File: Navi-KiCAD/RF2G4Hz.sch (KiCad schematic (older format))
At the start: 39 parts, among them J5 0734120110, U3 CC2650F128RGZR, U4 CC2592RGVR, Y5 XRCGB24M000F2P00R0

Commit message: Some BOM consolidation.
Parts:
- C37: value 1n -> 0.01u
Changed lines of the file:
@@
-$EndComp
-$Comp
-L GND #PWR093
-U 1 1 58AB4906
-P 7150 1200
-F 0 "#PWR093" H 7150 950 50  0001 C CNN
-F 1 "GND" H 7150 1050 50  0000 C CNN
-F 2 "" H 7150 1200 50  0001 C CNN
-F 3 "" H 7150 1200 50  0001 C CNN
-	1    7150 1200
-	1    0    0    -1
 $EndComp
 $Comp
@@
 F 7 "0402" H 250 -250 60  0001 L CNN "Package"
 	1    6750 1050
-	1    0    0    -1
-$EndComp
-$Comp
-L C C37
-U 1 1 58B661C8
-P 7150 1050
-F 0 "C37" H 7265 1096 50  0000 L CNN
-F 1 "1n" H 7265 1005 50  0000 L CNN
-F 2 "Capacitors_SMD:C_0402" H 638 -250 50  0001 C CNN
-F 3 "" H 600 -100 50  0001 C CNN
-F 4 "16V" H 700 -150 60  0001 L CNN "Voltage"
-F 5 "20%" H 700 -50 60  0001 L CNN "Tolerance"
-F 6 "X7R" H 650 50  60  0001 L CNN "Type"
-F 7 "0402" H 650 -250 60  0001 L CNN "Package"
-	1    7150 1050
 	1    0    0    -1
 $EndComp
@@
 Connection ~ 6400 900
 Connection ~ 6750 900
-Connection ~ 7150 900
 Wire Wire Line
 	1200 3450 1200 3550
@@
 	0    1    1    0
 $EndComp
+$Comp
+L GND #PWR093
+U 1 1 58AB4906
+P 7150 1200
+F 0 "#PWR093" H 7150 950 50  0001 C CNN
+F 1 "GND" H 7150 1050 50  0000 C CNN
+F 2 "" H 7150 1200 50  0001 C CNN
+F 3 "" H 7150 1200 50  0001 C CNN
+	1    7150 1200
+	1    0    0    -1
+$EndComp
+Connection ~ 7150 900
+$Comp
+L C C37
+U 1 1 58B661C8
+P 7150 1050
+F 0 "C37" H 7265 1096 50  0000 L CNN
+F 1 "0.01u" H 7265 1005 50  0000 L CNN
+F 2 "Capacitors_SMD:C_0402" H 638 -250 50  0001 C CNN
+F 3 "" H 600 -100 50  0001 C CNN
+F 4 "16V" H 700 -150 60  0001 L CNN "Voltage"
+F 5 "20%" H 700 -50 60  0001 L CNN "Tolerance"
+F 6 "X7R" H 650 50  60  0001 L CNN "Type"
+F 7 "0402" H 650 -250 60  0001 L CNN "Package"
+	1    7150 1050
+	1    0    0    -1
+$EndComp
 $EndSCHEMATC

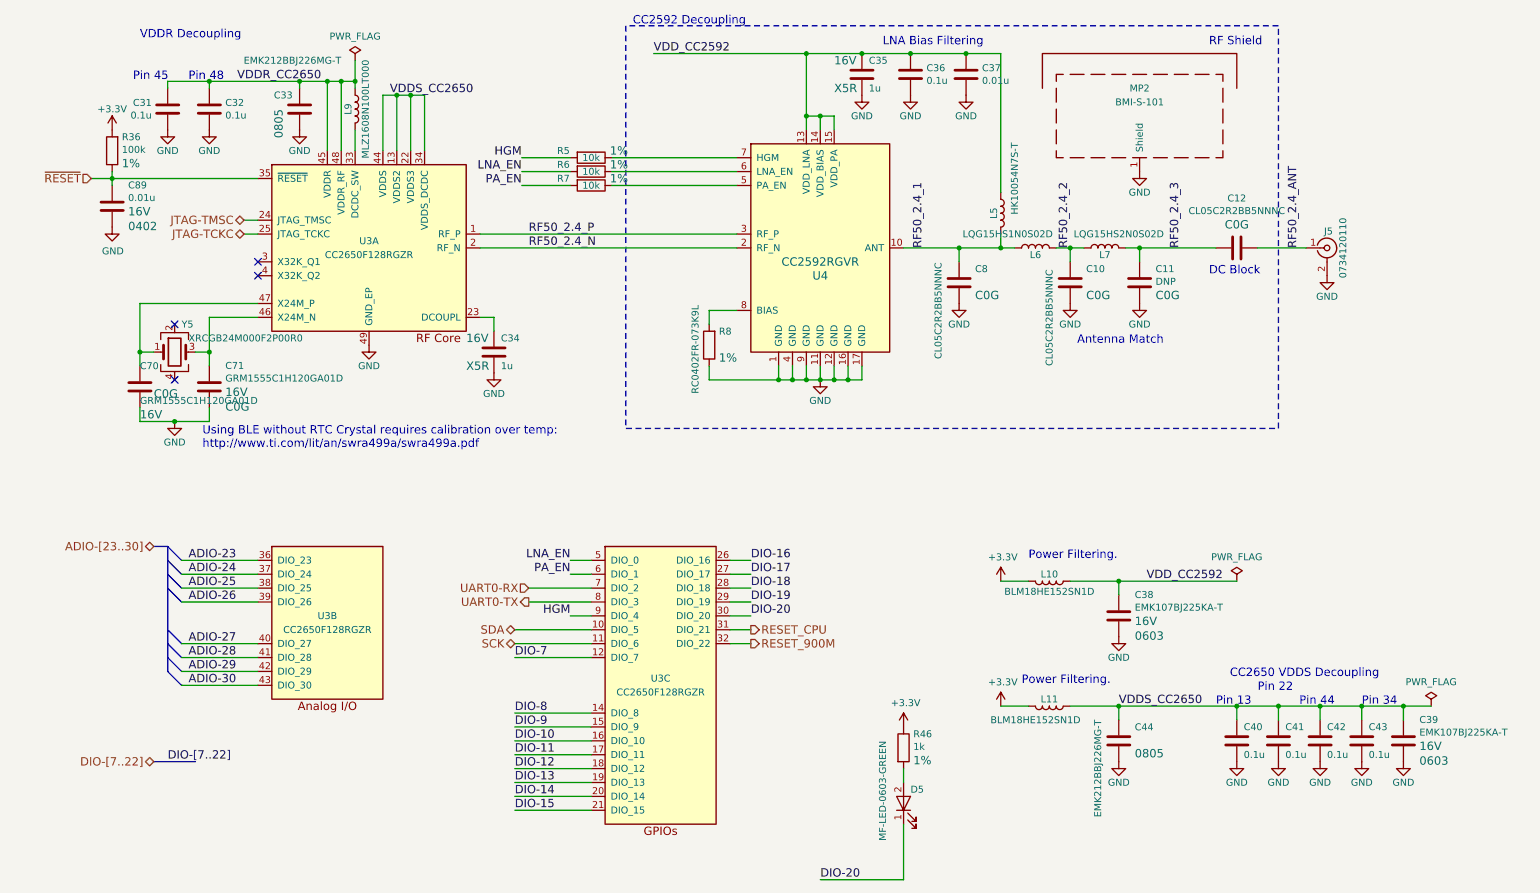
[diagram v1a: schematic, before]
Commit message: Completed key routing.
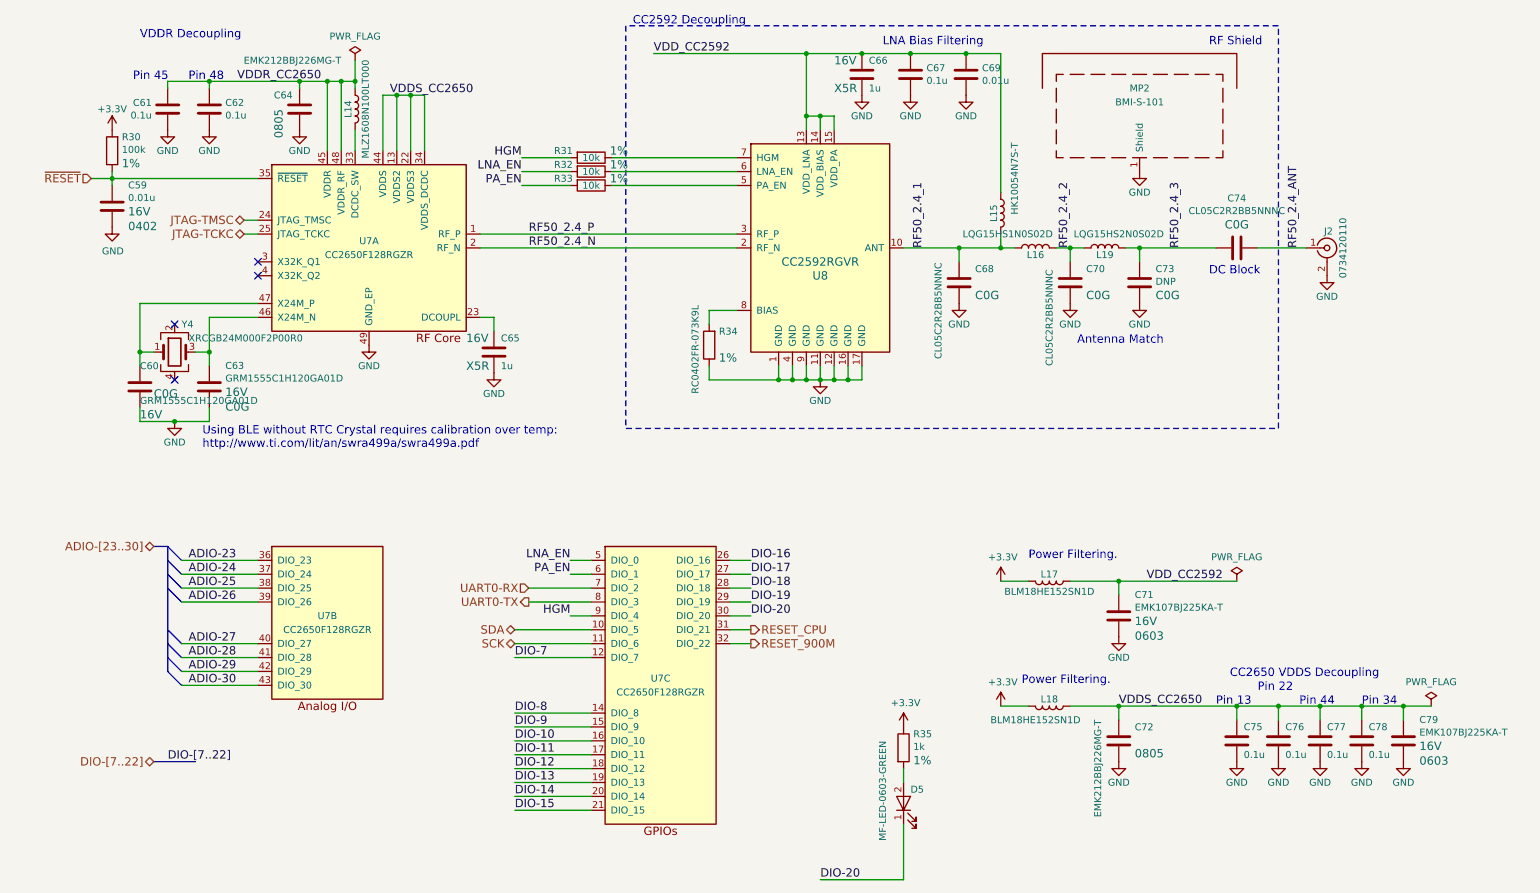
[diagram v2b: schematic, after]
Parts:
- renumbered C89 to C59, C70 to C60, C31 to C61, C32 to C62, C71 to C63, C33 to C64, C34 to C65, C35 to C66, C36 to C67, C8 to C68, C37 to C69, C10 to C70, C38 to C71, C44 to C72, C11 to C73, C12 to C74, C40 to C75, C41 to C76, C42 to C77, C43 to C78, C39 to C79, J5 to J2, L9 to L14, L5 to L15, L6 to L16, L10 to L17, L11 to L18, L7 to L19, R36 to R30, R5 to R31, R6 to R32, R7 to R33, R8 to R34, R46 to R35, U3 to U7, U4 to U8, Y5 to Y4
